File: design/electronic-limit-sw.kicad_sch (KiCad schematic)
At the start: 35 parts, among them J1 3.5mm - 2-pin screw terminal, J2 3.5mm - 2-pin screw terminal, J3 SMD - 2.54mm 4-pin pad termin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, J4 7.62mm - 4-pin screw terminal, Q1 MMBT2222, U1 PIC10F200-IOT

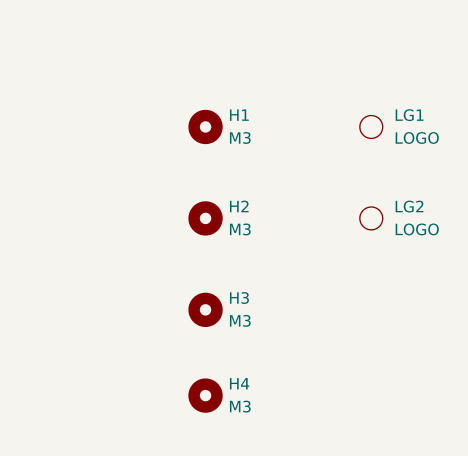
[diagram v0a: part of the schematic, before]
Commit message: Upgrade project to new KiCAD version.
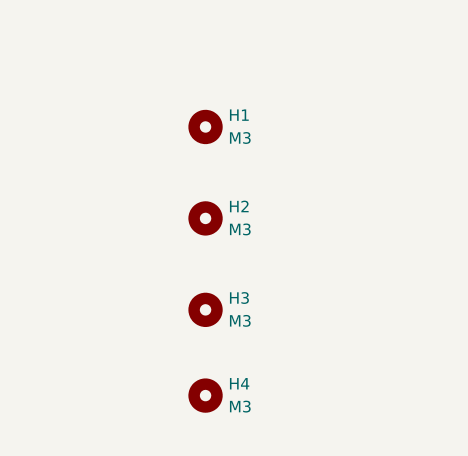
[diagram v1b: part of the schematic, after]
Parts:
- removed LG1: LOGO, simtelic:simtelic-name-5, symbol elect-generic-ic:LOGO
- removed LG2: LOGO, simtelic:simtelic-5, symbol elect-generic-ic:LOGO
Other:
- company: simtelic.com -> Dilshan Jayakody
